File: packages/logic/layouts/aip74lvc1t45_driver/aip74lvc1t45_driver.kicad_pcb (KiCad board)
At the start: 2 copper layers, 3 parts

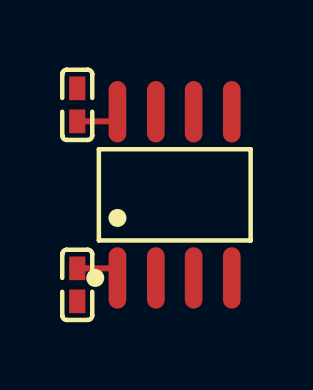
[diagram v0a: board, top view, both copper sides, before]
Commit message: Cleaning-up and updating to latest standards (#23)
* Update packages:

- add required flag
- package > driver method
- cleaning up
- aligning packages

* Rebuild all
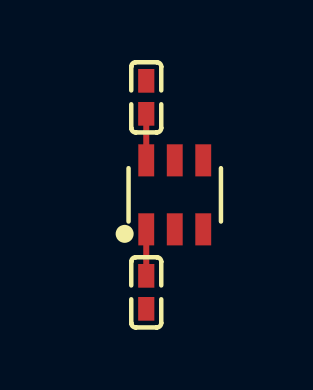
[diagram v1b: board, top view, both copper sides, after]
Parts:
- U1: footprint atopile:SOIC-8_L4.9-W3.9-P1.27-LS6.0-BL-6ccfeb -> atopile:SOT-23-6_L2.9-W1.6-P0.95-LS2.8-BL-d2c740
- moved C1 6.66 mm to (-0.95, 3.25), turned to -90 degrees
- moved C2 6.66 mm to (-0.95, -3.25), turned to 90 degrees
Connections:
- net line renamed buffer-line-2
- C1 pad 2: gnd-1 -> gnd
- U1 pad 1: hv -> hv-1
- U1 pad 2: line-3 -> gnd
- U1 pad 4: gnd -> buffer-line
- U1 pad 5: gnd-1 -> buffer-line-1
- U1 pad 6: line-2 -> hv

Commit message: WIP update logic
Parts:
- C1, C2: footprint atopile:C0402-b3ef17 -> Samsung_Electro_Mechanics_CL05B104KO5NNNC:C0402
- U1: footprint atopile:SOT-23-6_L2.9-W1.6-P0.95-LS2.8-BL-d2c740 -> Wuxi_I_core_Elec_AiP74LVC1T45GB236_TR:SOT-23-6_L2.9-W1.6-P0.95-LS2.8-BL
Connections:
- C1 pad 1: hv-1 -> hv
- C2 pad 1: hv -> hv-1
- U1 pad 1: hv-1 -> hv
- U1 pad 4: buffer-line -> buffer-line-1
- U1 pad 5: buffer-line-1 -> buffer-line
- U1 pad 6: hv -> hv-1

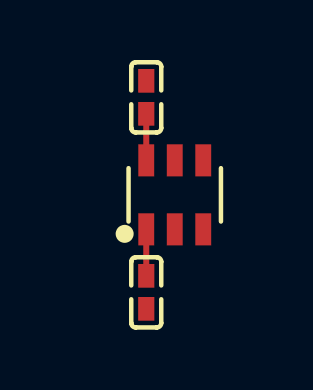
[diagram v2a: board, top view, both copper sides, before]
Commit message: Update 3D model locations
fix missing renders
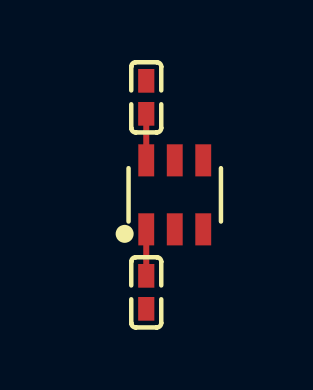
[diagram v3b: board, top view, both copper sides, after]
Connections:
- C1 pad 1: hv -> hv-1
- C2 pad 1: hv-1 -> hv
- U1 pad 1: hv -> hv-1
- U1 pad 3: buffer-line-2 -> buffer-line-1
- U1 pad 4: buffer-line-1 -> buffer-line
- U1 pad 5: buffer-line -> buffer-line-2
- U1 pad 6: hv-1 -> hv

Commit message: rebuild all packages & regenerate images of changed layouts (silk)
Add new scripts for version bump and build (based on atopile/packages)
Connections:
- C1 pad 1: hv-1 -> hv
- C2 pad 1: hv -> hv-1
- U1 pad 1: hv-1 -> hv
- U1 pad 4: buffer-line -> buffer-line-2
- U1 pad 5: buffer-line-2 -> buffer-line
- U1 pad 6: hv -> hv-1
